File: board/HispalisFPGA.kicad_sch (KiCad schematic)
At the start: 119 parts, among them J1 Conn_02x03_Odd_Even, J2 Conn_01x02_Socket, J3 USBC, J7 Conn_01x06, SW1 SW_Push, SW2 SW_DIP_x08, U1 LFE5UM-285, U10 PUSB3FR4Z, U11 PUSB3FR4Z, U12 LTC-4627JR, U2 S27KS0641DPBHI020, U3 DSC6001CI2A-016.0000T, U4 FAN53555UC04X, U5 MIC5504-2.5YMT-TR, U6 Conn_02x03_Counter_Clockwise, U7 FAN53600, U8 S25FL064L, U9 MIC5504-1.2YMT-TR

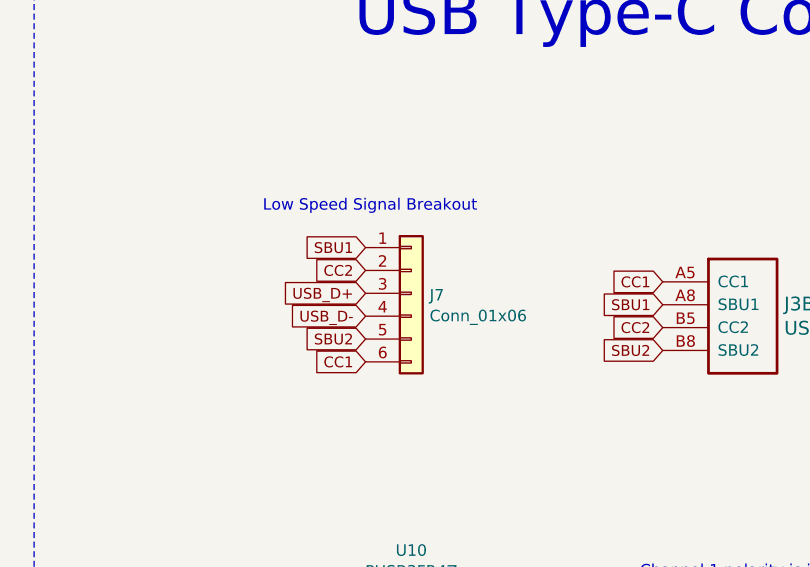
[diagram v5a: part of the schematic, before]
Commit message: Simplify USB connections
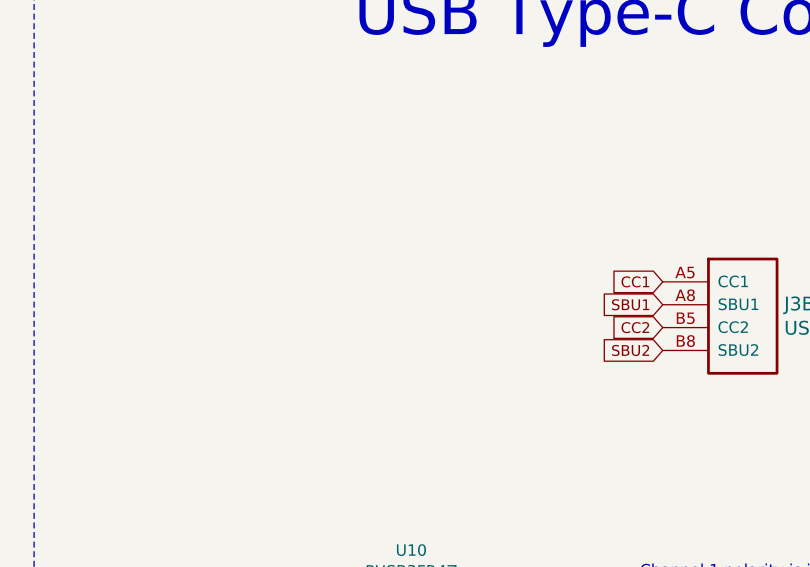
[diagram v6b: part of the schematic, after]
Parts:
- removed J7: Conn_01x06, symbol Connector_Generic:Conn_01x06
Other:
- note removed: "Low Speed Signal Breakout"
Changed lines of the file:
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@@
 		)
 	)
-	(text "Low Speed Signal Breakout"
-		(exclude_from_sim no)
-		(at 389.89 45.72 0)
-		(effects
-			(font
-				(size 1.27 1.27)
-			)
-			(justify left bottom)
-		)
-	)
 	(text "Channel 1 polarity is inverted"
 		(exclude_from_sim no)
@@
 		)
 	)
-	(global_label "USB_D-"
-		(shape input)
-		(at 401.32 57.15 180)
-		(effects
-			(font
-				(size 1.1938 1.1938)
-			)
-			(justify right)
-		)
-		(property "Intersheetrefs" "${INTERSHEET_REFS}"
-			(at 401.32 57.15 0)
-			(effects
-				(font
-					(size 1.27 1.27)
-				)
-				(hide yes)
-			)
-		)
-	)
 	(global_label "SW1"
 		(shape input)
@@
 		)
 	)
-	(global_label "CC2"
-		(shape input)
-		(at 401.32 52.07 180)
-		(effects
-			(font
-				(size 1.1938 1.1938)
-			)
-			(justify right)
-		)
-		(property "Intersheetrefs" "${INTERSHEET_REFS}"
-			(at 401.32 52.07 0)
-			(effects
-				(font
-					(size 1.27 1.27)
-				)
-				(hide yes)
-			)
-		)
-	)
 	(global_label "PMOD4_10"
 		(shape bidirectional)
@@
 		)
 	)
-	(global_label "SBU2"
-		(shape input)
-		(at 401.32 59.69 180)
-		(effects
-			(font
-				(size 1.1938 1.1938)
-			)
-			(justify right)
-		)
-		(property "Intersheetrefs" "${INTERSHEET_REFS}"
-			(at 401.32 59.69 0)
-			(effects
-				(font
-					(size 1.27 1.27)
-				)
-				(hide yes)
-			)
-		)
-	)
 	(global_label "RAM_DQ6"
 		(shape input)
@@
 		)
 	)
-	(global_label "CC1"
-		(shape input)
-		(at 401.32 62.23 180)
-		(effects
-			(font
-				(size 1.1938 1.1938)
-			)
-			(justify right)
-		)
-		(property "Intersheetrefs" "${INTERSHEET_REFS}"
-			(at 401.32 62.23 0)
-			(effects
-				(font
-					(size 1.27 1.27)
-				)
-				(hide yes)
-			)
-		)
-	)
 	(global_label "LED1"
 		(shape passive)
@@
 		)
 	)
-	(global_label "USB_D+"
-		(shape input)
-		(at 401.32 54.61 180)
-		(effects
-			(font
-				(size 1.1938 1.1938)
-			)
-			(justify right)
-		)
-		(property "Intersheetrefs" "${INTERSHEET_REFS}"
-			(at 401.32 54.61 0)
-			(effects
-				(font
-					(size 1.27 1.27)
-				)
-				(hide yes)
-			)
-		)
-	)
 	(global_label "USB3_REFCLK_0"
 		(shape input)
@@
 		)
 	)
-	(global_label "SBU1"
-		(shape input)
-		(at 401.32 49.53 180)
-		(effects
-			(font
-				(size 1.1938 1.1938)
-			)
-			(justify right)
-		)
-		(property "Intersheetrefs" "${INTERSHEET_REFS}"
-			(at 401.32 49.53 0)
-			(effects
-				(font
-					(size 1.27 1.27)
-				)
-				(hide yes)
-			)
-		)
-	)
 	(global_label "SW3"
 		(shape input)
@@
 					(unit 1)
 				)
-			)
-		)
-	)
-	(symbol
-		(lib_id "Connector_Generic:Conn_01x06")
-		(at 406.4 54.61 0)
-		(unit 1)
-		(exclude_from_sim no)
-		(in_bom yes)
-		(on_board yes)
-		(dnp no)
-		(property "Reference" "J7"
-			(at 408.432 54.8132 0)
-			(effects
-				(font
-					(size 1.27 1.27)
-				)
-				(justify left)
-			)
-		)
-		(property "Value" "Conn_01x06"
-			(at 408.432 57.1246 0)
-			(effects
-				(font
-					(size 1.27 1.27)
-				)
-				(justify left)
-			)
-		)
-		(property "Footprint" ""
-			(at 406.4 54.61 0)
-			(effects
-				(font
-					(size 1.27 1.27)
-				)
-				(hide yes)
-			)
-		)
-		(property "Datasheet" "~"
-			(at 406.4 54.61 0)
-			(effects
-				(font
-					(size 1.27 1.27)
-				)
-				(hide yes)
-			)
-		)
-		(property "Description" ""
-			(at 406.4 54.61 0)
-			(effects
-				(font
-					(size 1.27 1.27)
-				)
-				(hide yes)
-			)
-		)
-		(pin "6"
-		)
-		(pin "4"
-		)
-		(pin "5"
-		)
-		(pin "3"
-		)
-		(pin "2"
-		)
-		(pin "1"
-		)
-		(instances
-			(project "HispalisFPGA"
-				(path "/864346d0-d3ef-428e-a44f-9476f195db98"
-					(reference "J7")
-					(unit 1)
-				)

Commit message: Assign generic footprints
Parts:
- C10, C11, C12, C13, C14, C15, C16, C17, C18, C19, C20, C24, C26, C28, C29, C3, C30, C31, C34, C35, C36, C37, C38, C39, C4, C40, C41, C42, C43, C44, C45, C46, C47, C6, C7, C8, C9: footprint Footprints:C_0402_NoSilk -> Capacitor_SMD:C_0402_1005Metric
- C22, C23, C5: footprint Capacitors_SMD:C_0603 -> Capacitor_SMD:C_0603_1608Metric
- D1, D2: footprint LEDs:LED_0603 -> LED_SMD:LED_0603_1608Metric
- L1: footprint Inductors_SMD:L_Vishay_IHLP-1616 -> Inductor_SMD:L_2512_6332Metric
- L2: footprint Inductors_SMD:L_Wuerth_MAPI-2010 -> Inductor_SMD:L_2010_5025Metric
- PMOD2, PMOD3, PMOD4: footprint (none) -> Connector_PinSocket_2.54mm:PinSocket_2x06_P2.54mm_Horizontal
- R10, R11, R12, R13, R4, R5, R7: footprint Footprints:R_0402_NoSilk -> Resistor_SMD:R_0402_1005Metric
- R31, R32, R33, R34, R35, R36, R37, R38: footprint (none) -> Resistor_SMD:R_0402_1005Metric
- SW1: footprint Footprints:PTS_810_SMT_Switch -> Button_Switch_THT:SW_PUSH_6mm
- TP1, TP11, TP12, TP13: footprint Footprints:small-testpoint -> TestPoint:TestPoint_Pad_D1.0mm; symbol HispalisFPGA-rescue:Test_Point-Connector -> Connector:TestPoint
- U1: footprint (none) -> Footprints:csfBGA 285
- U10, U11: footprint (none) -> Footprints:PUSB3FR4Z
- U5, U9: footprint Footprints:Thin-DFN4 -> Package_DFN_QFN:UDFN-4-1EP_1x1mm_P0.65mm_EP0.48x0.48mm

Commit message: Cleanup unused symbols
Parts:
- C10, C11, C12, C13, C14, C15, C16, C17, C18, C19, C20, C22, C23, C24, C26, C28, C29, C3, C30, C31, C34, C35, C36, C37, C38, C39, C4, C40, C41, C42, C43, C44, C45, C46, C47, C5, C6, C7, C8, C9: symbol Device:C_Small -> Device:C
- J3: symbol HispalisFPGA-rescue:USBC-Components -> HispalisFPGA:USBC-Components
- L1, L2: symbol Device:L_Small -> Device:L
- R10, R11, R12, R13, R4, R5, R7: symbol Device:R_Small -> Device:R
- U1: symbol HispalisFPGA-rescue:LFE5UM-285-Components -> HispalisFPGA:LFE5UM-285-Components
- U2: symbol HispalisFPGA-rescue:S27KS0641DPBHI020-Components -> HispalisFPGA:S27KS0641DPBHI020-Components
- U3: symbol HispalisFPGA-rescue:DSC6001CI2A-016.0000T-Components -> HispalisFPGA:DSC6001CI2A-016.0000T-Components
- U4: symbol HispalisFPGA-rescue:FAN53555-Components -> HispalisFPGA:FAN53555-Components
- U5: symbol HispalisFPGA-rescue:MIC5504-2.5YM5-TR-Components -> HispalisFPGA:MIC5504-2.5YM5-TR-Components
- U7: symbol HispalisFPGA-rescue:FAN53600-Components -> HispalisFPGA:FAN53600-Components
- U8: symbol HispalisFPGA-rescue:S25FL064L-Components -> HispalisFPGA:S25FL064L-Components
- U9: symbol HispalisFPGA-rescue:MIC5504-1.8YM5-TR-Components -> HispalisFPGA:MIC5504-1.8YM5-TR-Components
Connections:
- net +1V1: no longer C10.1, C12.1, C13.1, C14.1, C15.1, C16.1, C22.1, L1.2
- net +1V2: no longer C36.1, C37.1, C38.1, C39.1, C40.1, C41.1, C43.1
- net +2V5: no longer C20.1, C6.1, C7.1
- net +3V3: no longer C11.1, C17.1, C18.1, C24.1, C26.1, C28.1, C29.1, C3.1, C30.1, C31.1, C34.1, C35.1, C4.1, C42.1, C9.1, L2.2, R10.1, R5.1
- net +5V: no longer C19.1, C5.1, C8.1
- net CFG_MODE_SEL_0: no longer R7.1
- net CFG_MODE_SEL_1: no longer R5.2
- net CH0_TXN: no longer C47.2
- net CH0_TXP: no longer C45.2
- net CH1_TXN: no longer C46.2
- net CH1_TXP: no longer C44.2
- net GND: no longer C10.2, C11.2, C12.2, C13.2, C14.2, C15.2, C16.2, C17.2, C18.2, C19.2, C20.2, C22.2, C23.2, C24.2, C26.2, C28.2, C29.2, C3.2, C30.2, C31.2, C34.2, C35.2, C36.2, C37.2, C38.2, C39.2, C4.2, C40.2, C41.2, C42.2, C43.2, C5.2, C6.2, C7.2, C8.2, C9.2, R12.2, R13.2
- net PROGRAMN: no longer R10.2
- net TCK: no longer R4.1
- net USB_CONNECT: no longer R11.1
- net USB_D+: no longer R11.2
- net at L2.1: no longer U7.B1 (SW)
- net at U4.D3 (SW[4]), U4.D4 (SW[4]), U4.E3 (SW[4])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: no longer L1.1
- net at D1.1 (K): no longer R12.1
- net at R13.1: no longer D2.1 (K)
- net at C46.1: no longer J3.A2 (TX1+)
- net at C44.1: no longer J3.A3 (TX1-)
- net at C47.1: no longer J3.B3 (TX2-)
- net at C45.1: no longer J3.B2 (TX2+)
